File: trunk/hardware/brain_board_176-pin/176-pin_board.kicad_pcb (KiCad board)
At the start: 4 copper layers, 61.8 x 73.2 mm, 76 parts, among them J1 MINI-USB-5P-3400020P1, P1 CONN_25X2, P10 CONN_2X2, P11 CONN_4X2, P12 CONN_4X2, P13 CONN_8X2, P2 CONN_25X2, P3 CONN_2, P4 CONN_6, P5 CONN_1, P6 CONN_2X2, P7 CONN_4X2, P8 CONN_4X2, P9 CONN_4X2, SW1 SW_PUSH, U1 STM32F407IGT6, U2 NUF2101MT1G, U3 LM2937, X1 CRYSTAL, X2 CRYSTAL

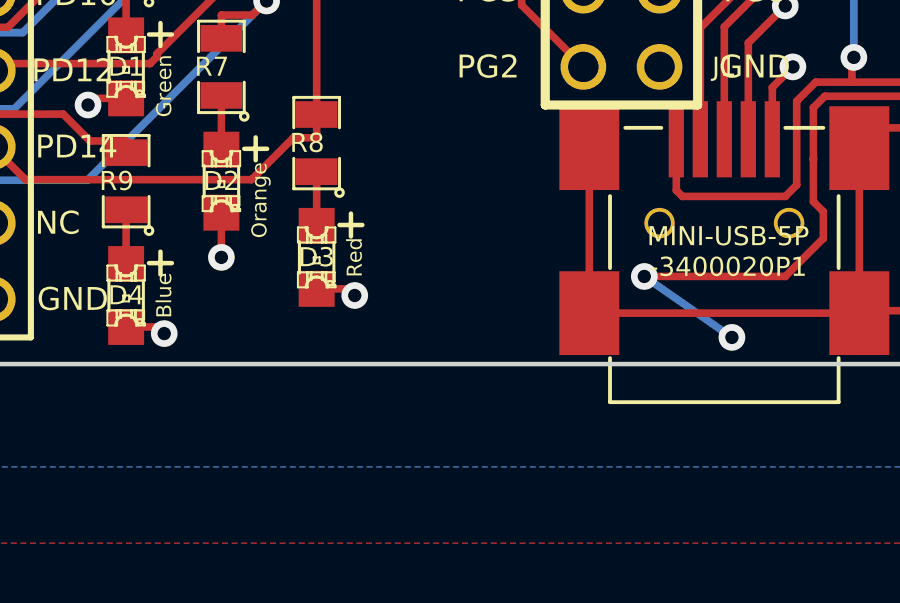
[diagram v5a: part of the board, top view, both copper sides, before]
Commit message: 
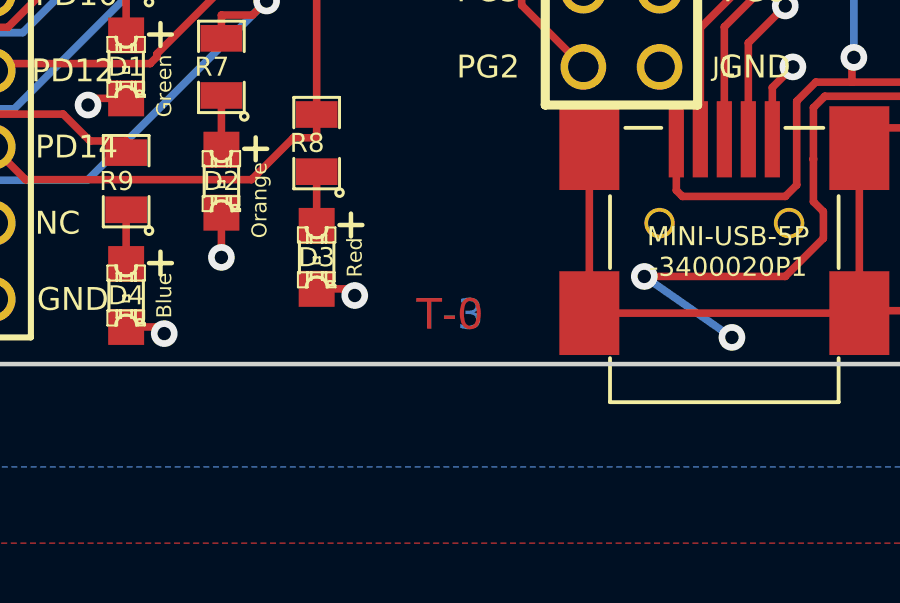
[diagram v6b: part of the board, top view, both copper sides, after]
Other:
- board text added: "4 layer board stackup is as follows: T-0 is top 1 oz copper (1.4 mil) 6.7 mil prepreg FR4 T-1 is GND 0.5 oz copper (0.7 mil) 47 mil core FR4 T-2 is PWR 0.5 oz copper (0.7 mil) 6.7 mil prepreg FR4 T-3 is bottom 1 oz copper (1.4 mil)"
- board text added: "T-0"
- board text added: "T-1"
- board text added: "T-2"
- board text added: "T-3"
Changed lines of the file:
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@@
     (links 314)
     (no_connects 0)
-    (area 69.947674 61.494999 160.020001 171.672001)
+    (area 69.947674 61.494999 160.020001 182.753)
     (thickness 1.6)
-    (drawings 330)
+    (drawings 336)
     (tracks 1858)
     (zones 0)
@@
     (visible_elements 7FFFFB3F)
     (pcbplotparams
-      (layerselection 284983297)
+      (layerselection 301760519)
       (usegerberextensions true)
       (excludeedgelayer true)
@@
     )
   )
+  (gr_line (start 109.22 157.48) (end 109.22 167.64) (angle 90) (layer Dwgs.User) (width 0.2))
+  (gr_text "4 layer board stackup is as follows: \nT-0 is top 1 oz copper (1.4 mil)\n6.7 mil prepreg FR4\nT-1 is GND 0.5 oz copper (0.7 mil)\n47 mil core FR4\nT-2 is PWR 0.5 oz copper (0.7 mil)\n6.7 mil prepreg FR4\nT-3 is bottom 1 oz copper (1.4 mil)" (at 111.76 170.18) (layer Dwgs.User)
+    (effects (font (size 1.016 1.016) (thickness 0.254)))
+  )
+  (gr_text T-3 (at 109.22 154.94) (layer B.Cu)
+    (effects (font (size 1.016 1.016) (thickness 0.254)))
+  )
+  (gr_text T-2 (at 109.22 154.94) (layer PWR)
+    (effects (font (size 1.016 1.016) (thickness 0.254)))
+  )
+  (gr_text T-1 (at 109.22 154.94) (layer GND)
+    (effects (font (size 1.016 1.016) (thickness 0.254)))
+  )
+  (gr_text T-0 (at 109.22 154.94) (layer F.Cu)
+    (effects (font (size 1.016 1.016) (thickness 0.254)))
+  )
   (gr_text "STM\nVBAT" (at 134.62 94.615) (layer B.SilkS)

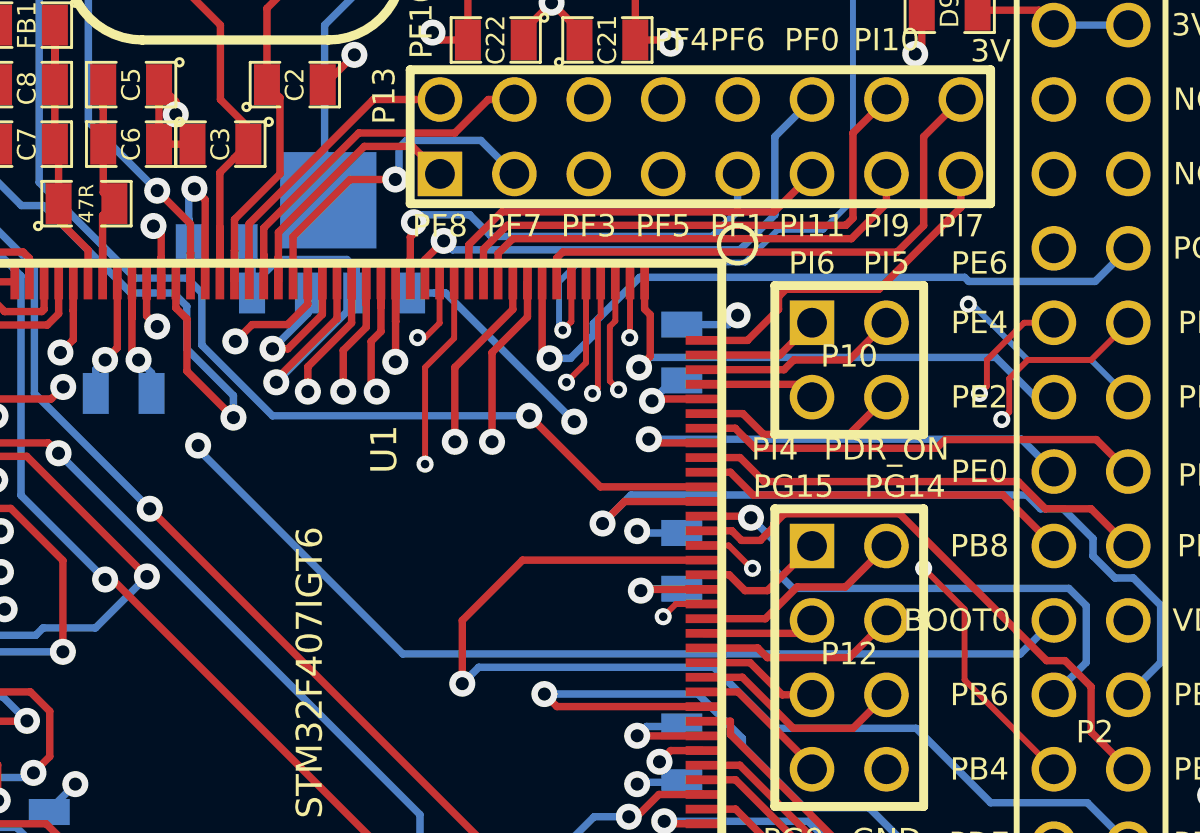
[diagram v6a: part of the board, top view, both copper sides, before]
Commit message: 
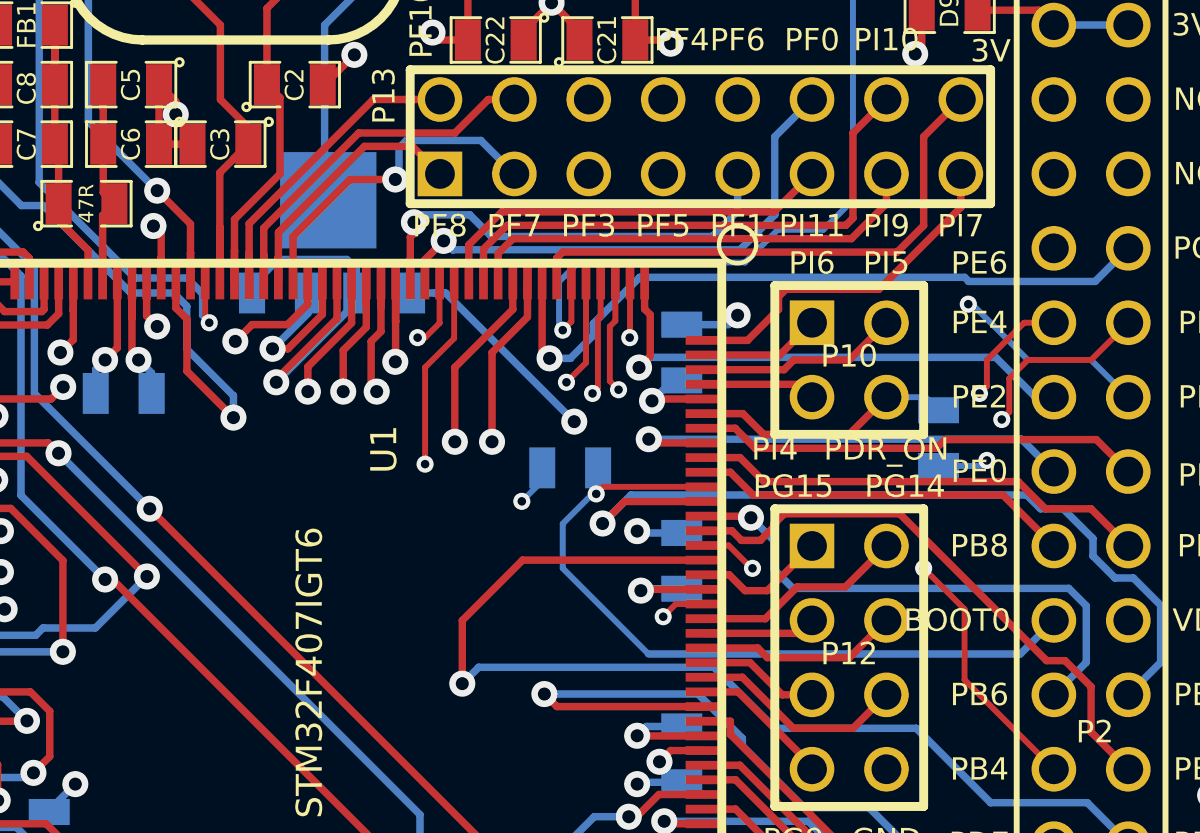
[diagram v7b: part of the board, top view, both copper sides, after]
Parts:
- added R1: 1k, SM0805, B.Cu at (138.3, 112.6)
- moved R4 14.3 mm to (125.7, 113.7), turned to 0 degrees
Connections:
- U1 pad 166: /NRST -> /BOOT0
- U1 pad 31: /BOOT0 -> /NRST
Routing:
- net /BOOT0: track 47.7 -> 26.2 mm, vias 2 -> 1
- net /NRST: track 71.0 -> 52.7 mm
- net /PDR_ON: track 7.08 -> 9.04 mm
- net /VDD: track 80.2 -> 81.9 mm, vias 22 -> 23
- net GND: vias 41 -> 42

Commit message: progress
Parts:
- added W1: TEST, SIL-2, F.Cu at (97.8, 113.7)
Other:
- net class Default: clearance 0.2032 -> 0.1778
- rule trace_clearance: 0.2032 -> 0.1778
